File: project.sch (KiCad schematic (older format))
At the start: 68 parts, among them J1 USB3_B, J2 Jumper_3_Open, J3 Jumper_3_Open, J4 Jumper_3_Open, J6 Conn_02x10_Odd_Even, SW1 SW_Push, U1 CYUSB3014, U2 Conn_02x32_Odd_Even, U3 M25P80, U4 MP2359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

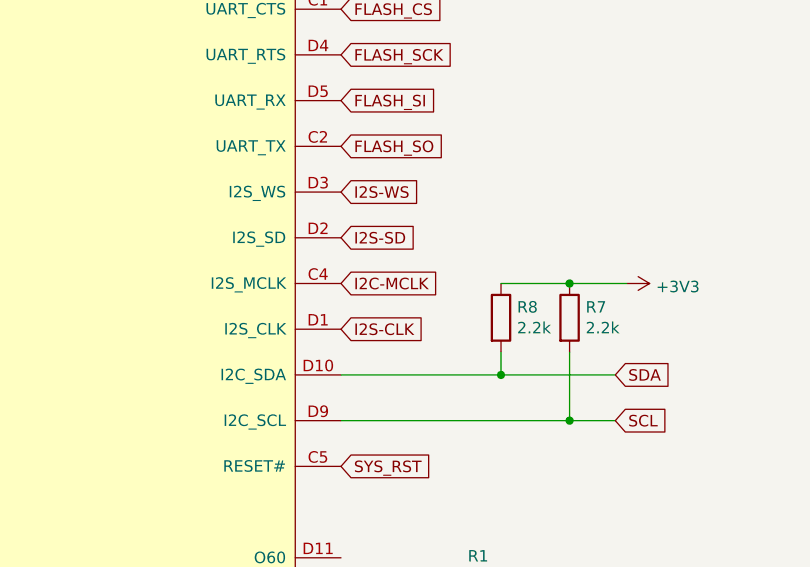
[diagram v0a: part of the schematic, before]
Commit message: everything routed
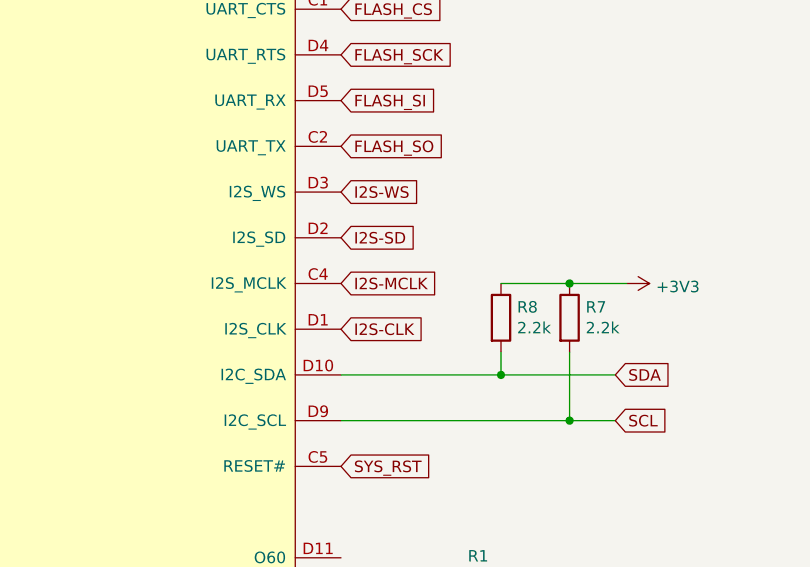
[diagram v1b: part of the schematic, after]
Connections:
- net I2C-MCLK is gone; now on net I2S-MCLK: U1.C4 (I2S_MCLK)
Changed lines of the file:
@@
 FLASH_SI
 Text GLabel 14900 11600 2    50   Input ~ 0
-I2C-MCLK
+I2S-MCLK
 Text GLabel 14900 10000 2    50   Input ~ 0
 SS_RX_P
